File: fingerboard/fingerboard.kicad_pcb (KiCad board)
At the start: 2 copper layers, 36 x 76 mm, 12 parts, among them J1 Conn_01x10, SW1 SW_Push, SW2 SW_Push, SW3 SW_Push, SW4 SW_Push, SW5 SW_Push, SW6 SW_Push, SW7 SW_Push, SW8 SW_Push

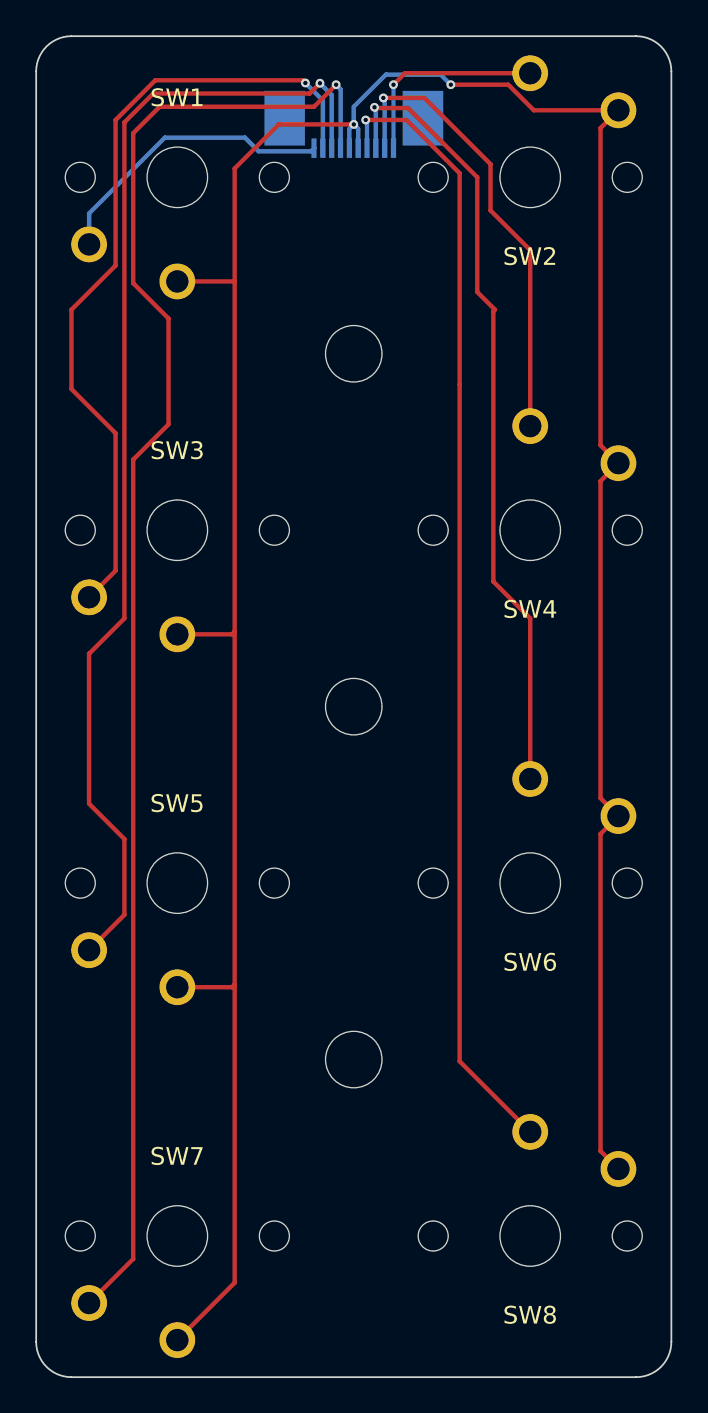
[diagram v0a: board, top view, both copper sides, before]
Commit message: Overhaul fingerboard (incl vertical connector)
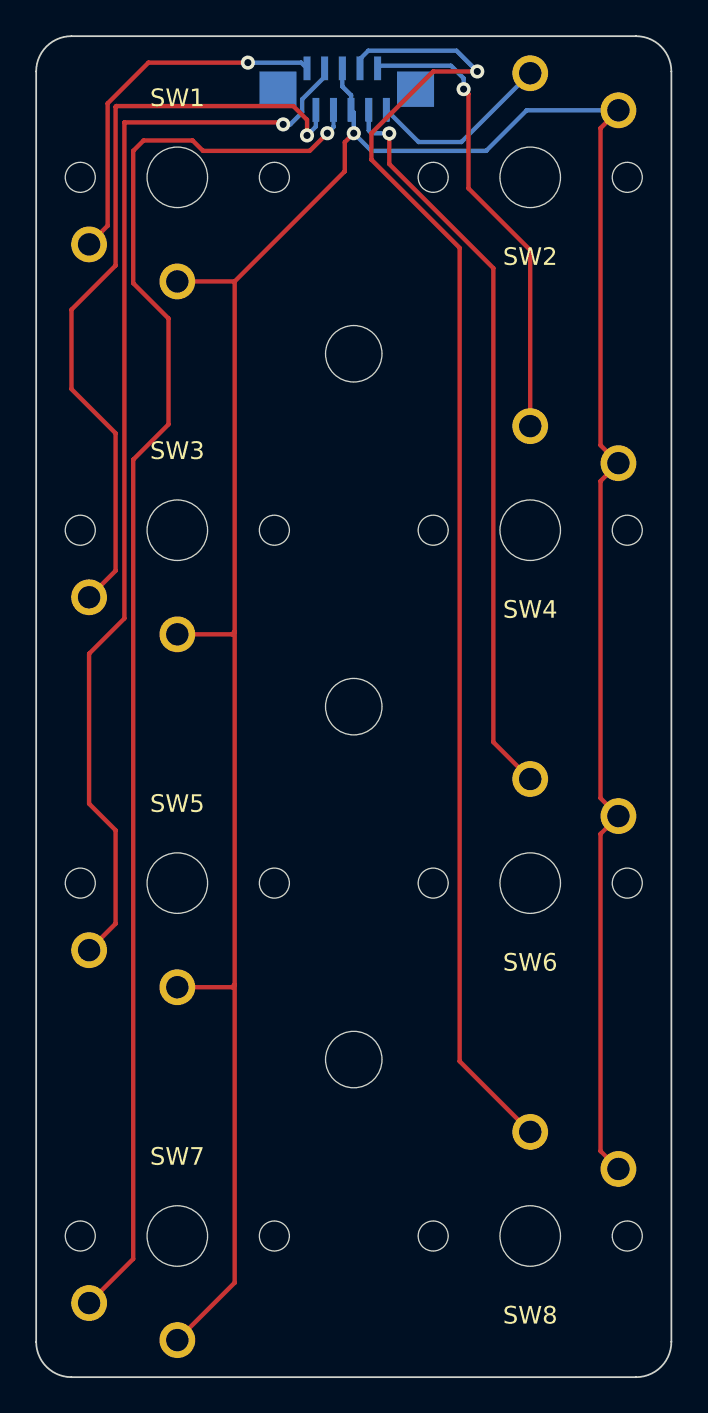
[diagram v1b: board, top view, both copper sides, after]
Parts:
- J1: footprint Connector_FFC-FPC:TE_1-1734839-0_1x10-1MP_P0.5mm_Horizontal -> Custom:GCT_FFC2A33-10-T-R_REVA_MPs
- moved J1 2.04 mm to (119.6, 45.0)
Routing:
- net COL8: track 64.2 -> 75.6 mm
- net COL1: track 16.7 -> 20.8 mm, vias 0 -> 1
- net COL7: track 85.3 -> 81.4 mm
- net COL5: track 65.4 -> 62.4 mm
- net COL6: track 45.2 -> 42.3 mm
- net GND: track 168.4 -> 165.7 mm, vias 2 -> 1
- net COL3: track 45.6 -> 44.2 mm
- net COL2: track 11.6 -> 10.5 mm, vias 1 -> 0

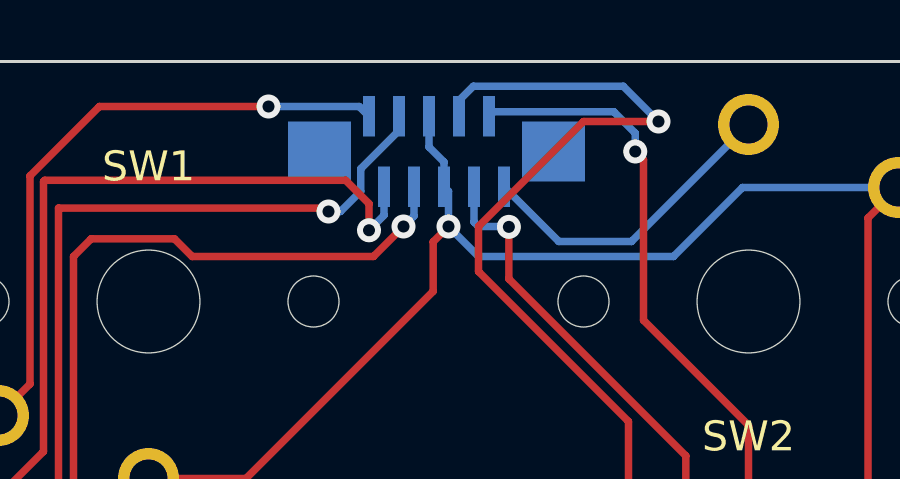
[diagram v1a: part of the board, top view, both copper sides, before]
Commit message: Center fingerboard connector (fraction of a millimeter, not really a practical difference) and put grid origin somewhere useful
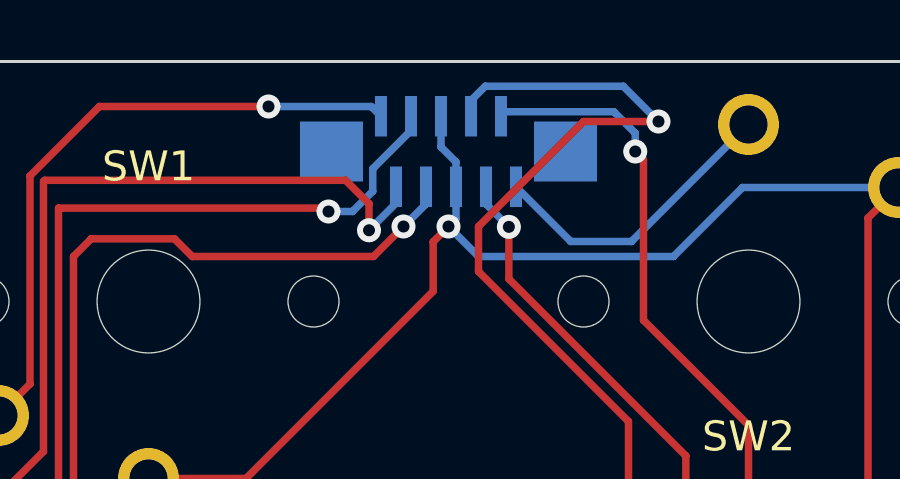
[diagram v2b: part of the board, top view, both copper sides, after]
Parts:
- moved J1 0.40 mm to (120.0, 45.0)
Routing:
- net COL6: track 42.3 -> 41.5 mm
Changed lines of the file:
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@@
     )
     (pad_to_mask_clearance 0)
+    (grid_origin 120 80)
     (pcbplotparams
       (layerselection 0x00010f4_ffffffff)
@@
   )
   (footprint "Custom:GCT_FFC2A33-10-T-R_REVA_MPs" (layer "B.Cu")
-    (at 119.6 45)
+    (at 120 45)
     (property "Sheetfile" "fingerboard.kicad_sch")
     (property "Sheetname" "")
@@
   (segment (start 108.363604 43.5) (end 114 43.5) (width 0.25) (layer "F.Cu") (net 1))
   (via (at 114 43.5) (size 0.8) (drill 0.4) (layers "F.Cu" "B.Cu") (net 1))
-  (segment (start 114 43.5) (end 117.025 43.5) (width 0.25) (layer "B.Cu") (net 1))
-  (segment (start 117.025 43.5) (end 117.35 43.825) (width 0.25) (layer "B.Cu") (net 1))
+  (segment (start 114.4 43.5) (end 117.425 43.5) (width 0.25) (layer "B.Cu") (net 1))
+  (segment (start 117.425 43.5) (end 117.75 43.825) (width 0.25) (layer "B.Cu") (net 1))
   (segment (start 117.349951 46.737701) (end 116.572099 45.959849) (width 0.25) (layer "F.Cu") (net 2))
   (segment (start 104 57.5) (end 104 62) (width 0.25) (layer "F.Cu") (net 2))
@@
   (segment (start 106.5 55) (end 104 57.5) (width 0.25) (layer "F.Cu") (net 2))
   (via (at 117.349951 47.625451) (size 0.8) (drill 0.4) (layers "F.Cu" "B.Cu") (net 2))
-  (segment (start 117.349951 47.625451) (end 117.85 47.125402) (width 0.25) (layer "B.Cu") (net 2))
-  (segment (start 117.85 47.125402) (end 117.85 46.175) (width 0.25) (layer "B.Cu") (net 2))
+  (segment (start 118.25 46.725402) (end 117.349951 47.625451) (width 0.25) (layer "B.Cu") (net 2))
+  (segment (start 118.25 46.175) (end 118.25 46.725402) (width 0.25) (layer "B.Cu") (net 2))
   (segment (start 107 46.886396) (end 107 75) (width 0.25) (layer "F.Cu") (net 3))
   (segment (start 105 85.5) (end 106.5 87) (width 0.25) (layer "F.Cu") (net 3))
@@
   (segment (start 106.5 92.3) (end 105 93.8) (width 0.25) (layer "F.Cu") (net 3))
   (via (at 116 47) (size 0.8) (drill 0.4) (layers "F.Cu" "B.Cu") (net 3))
-  (segment (start 116.4 47) (end 117.075 46.325) (width 0.25) (layer "B.Cu") (net 3))
-  (segment (start 117.075 46.325) (end 117.075 45.575) (width 0.25) (layer "B.Cu") (net 3))
-  (segment (start 116 47) (end 116.4 47) (width 0.25) (layer "B.Cu") (net 3))
-  (segment (start 118.35 44.3) (end 118.35 43.825) (width 0.25) (layer "B.Cu") (net 3))
-  (segment (start 117.075 45.575) (end 118.35 44.3) (width 0.25) (layer "B.Cu") (net 3))
+  (segment (start 116.8 47) (end 116 47) (width 0.25) (layer "B.Cu") (net 3))
+  (segment (start 117.475 46.325) (end 116.8 47) (width 0.25) (layer "B.Cu") (net 3))
+  (segment (start 117.475 46.325) (end 117.475 45.575) (width 0.25) (layer "B.Cu") (net 3))
+  (segment (start 118.75 44.3) (end 118.75 43.825) (width 0.25) (layer "B.Cu") (net 3))
+  (segment (start 117.475 45.575) (end 118.75 44.3) (width 0.25) (layer "B.Cu") (net 3))
   (segment (start 107.5 48.5) (end 107.5 56) (width 0.25) (layer "F.Cu") (net 4))
   (segment (start 117.5 48.5) (end 111.454999 48.5) (width 0.25) (layer "F.Cu") (net 4))
@@
   (segment (start 109.5 58) (end 109.5 64) (width 0.25) (layer "F.Cu") (net 4))
   (via (at 118.5 47.5) (size 0.8) (drill 0.4) (layers "F.Cu" "B.Cu") (net 4))
-  (segment (start 118.85 47.15) (end 118.85 46.175) (width 0.25) (layer "B.Cu") (net 4))
-  (segment (start 118.5 47.5) (end 118.85 47.15) (width 0.25) (layer "B.Cu") (net 4))
+  (segment (start 119.25 46.75) (end 118.5 47.5) (width 0.25) (layer "B.Cu") (net 4))
+  (segment (start 119.25 46.175) (end 119.25 46.75) (width 0.25) (layer "B.Cu") (net 4))
   (segment (start 113.25 75.75) (end 113.25 95.75) (width 0.25) (layer "F.Cu") (net 5))
   (segment (start 133.984001 87.215999) (end 135 86.2) (width 0.25) (layer "F.Cu") (net 5))
@@
   (segment (start 135 106.2) (end 133.984001 105.184001) (width 0.25) (layer "F.Cu") (net 5))
   (via (at 120 47.5) (size 0.8) (drill 0.4) (layers "F.Cu" "B.Cu") (net 5))
-  (segment (start 119.85 45.35) (end 119.85 46.175) (width 0.25) (layer "B.Cu") (net 5))
-  (segment (start 120 46.325) (end 119.85 46.175) (width 0.25) (layer "B.Cu") (net 5))
-  (segment (start 119.35 44.85) (end 119.85 45.35) (width 0.25) (layer "B.Cu") (net 5))
+  (segment (start 120.25 45.35) (end 120.25 46.175) (width 0.25) (layer "B.Cu") (net 5))
+  (segment (start 119.75 44.85) (end 120.25 45.35) (width 0.25) (layer "B.Cu") (net 5))
   (segment (start 129.8 46.2) (end 135 46.2) (width 0.25) (layer "B.Cu") (net 5))
-  (segment (start 120 47.5) (end 120 46.325) (width 0.25) (layer "B.Cu") (net 5))
   (segment (start 120 47.5) (end 121 48.5) (width 0.25) (layer "B.Cu") (net 5))
+  (segment (start 120.25 46.175) (end 120.25 47.25) (width 0.25) (layer "B.Cu") (net 5))
+  (segment (start 120.25 47.25) (end 120 47.5) (width 0.25) (layer "B.Cu") (net 5))
   (segment (start 127.5 48.5) (end 129.8 46.2) (width 0.25) (layer "B.Cu") (net 5))
-  (segment (start 119.35 43.825) (end 119.35 44.85) (width 0.25) (layer "B.Cu") (net 5))
+  (segment (start 119.75 43.825) (end 119.75 44.85) (width 0.25) (layer "B.Cu") (net 5))
   (segment (start 121 48.5) (end 127.5 48.5) (width 0.25) (layer "B.Cu") (net 5))
-  (segment (start 119.85 46.175) (end 119.85 46.65) (width 0.25) (layer "B.Cu") (net 5))
   (segment (start 121 47.5) (end 121 49) (width 0.25) (layer "F.Cu") (net 6))
   (segment (start 121 49) (end 126 54) (width 0.25) (layer "F.Cu") (net 6))
@@
   (segment (start 126 100.1) (end 130 104.1) (width 0.25) (layer "F.Cu") (net 6))
   (via (at 127 44) (size 0.8) (drill 0.4) (layers "F.Cu" "B.Cu") (net 6))
-  (segment (start 125.825 42.825) (end 120.825 42.825) (width 0.25) (layer "B.Cu") (net 6))
   (segment (start 127 44) (end 125.825 42.825) (width 0.25) (layer "B.Cu") (net 6))
-  (segment (start 120.35 43.3) (end 120.35 43.825) (width 0.25) (layer "B.Cu") (net 6))
-  (segment (start 120.825 42.825) (end 120.35 43.3) (width 0.25) (layer "B.Cu") (net 6))
+  (segment (start 121.225 42.825) (end 125.825 42.825) (width 0.25) (layer "B.Cu") (net 6))
+  (segment (start 120.75 43.3) (end 121.225 42.825) (width 0.25) (layer "B.Cu") (net 6))
+  (segment (start 120.75 43.825) (end 120.75 43.3) (width 0.25) (layer "B.Cu") (net 6))
   (segment (start 122.012299 47.512299) (end 122.012299 49.245983) (width 0.25) (layer "F.Cu") (net 7))
   (segment (start 127.9105 55.144184) (end 127.9105 82.0105) (width 0.25) (layer "F.Cu") (net 7))
@@
   (segment (start 127.9105 82.0105) (end 130 84.1) (width 0.25) (layer "F.Cu") (net 7))
   (via (at 122.012299 47.512299) (size 0.8) (drill 0.4) (layers "F.Cu" "B.Cu") (net 7))
-  (segment (start 122 47.5) (end 121 47.5) (width 0.25) (layer "B.Cu") (net 7))
-  (segment (start 120.85 47.35) (end 120.85 46.175) (width 0.25) (layer "B.Cu") (net 7))
-  (segment (start 122.012299 47.512299) (end 122 47.5) (width 0.25) (layer "B.Cu") (net 7))
-  (segment (start 121 47.5) (end 120.85 47.35) (width 0.25) (layer "B.Cu") (net 7))
+  (segment (start 121.25 46.175) (end 121.25 46.75) (width 0.25) (layer "B.Cu") (net 7))
+  (segment (start 121.25 46.75) (end 122.012299 47.512299) (width 0.25) (layer "B.Cu") (net 7))
   (segment (start 126.5 45.275) (end 126.5 50.625) (width 0.25) (layer "F.Cu") (net 8))
   (segment (start 126.5 50.625) (end 130 54.125) (width 0.25) (layer "F.Cu") (net 8))
@@
   (segment (start 126.225 45) (end 126.5 45.275) (width 0.25) (layer "F.Cu") (net 8))
   (via (at 126.225 45) (size 0.8) (drill 0.4) (layers "F.Cu" "B.Cu") (net 8))
-  (segment (start 125.511396 43.675) (end 121.5 43.675) (width 0.25) (layer "B.Cu") (net 8))
+  (segment (start 121.75 43.825) (end 121.9 43.675) (width 0.25) (layer "B.Cu") (net 8))
   (segment (start 126.225 44.388604) (end 125.511396 43.675) (width 0.25) (layer "B.Cu") (net 8))
   (segment (start 126.225 45) (end 126.225 44.388604) (width 0.25) (layer "B.Cu") (net 8))
-  (segment (start 121.5 43.675) (end 121.35 43.825) (width 0.25) (layer "B.Cu") (net 8))
+  (segment (start 121.9 43.675) (end 125.511396 43.675) (width 0.25) (layer "B.Cu") (net 8))
+  (segment (start 122.25 46.175) (end 124.075 48) (width 0.25) (layer "B.Cu") (net 9))
+  (segment (start 124.075 48) (end 126.1 48) (width 0.25) (layer "B.Cu") (net 9))
   (segment (start 126.1 48) (end 130 44.1) (width 0.25) (layer "B.Cu") (net 9))
-  (segment (start 121.85 46.175) (end 123.675 48) (width 0.25) (layer "B.Cu") (net 9))
-  (segment (start 123.675 48) (end 126.1 48) (width 0.25) (layer "B.Cu") (net 9))
 )
